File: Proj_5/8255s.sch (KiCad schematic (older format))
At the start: 18 parts, among them U1 8255, U2 8255, U3 8255

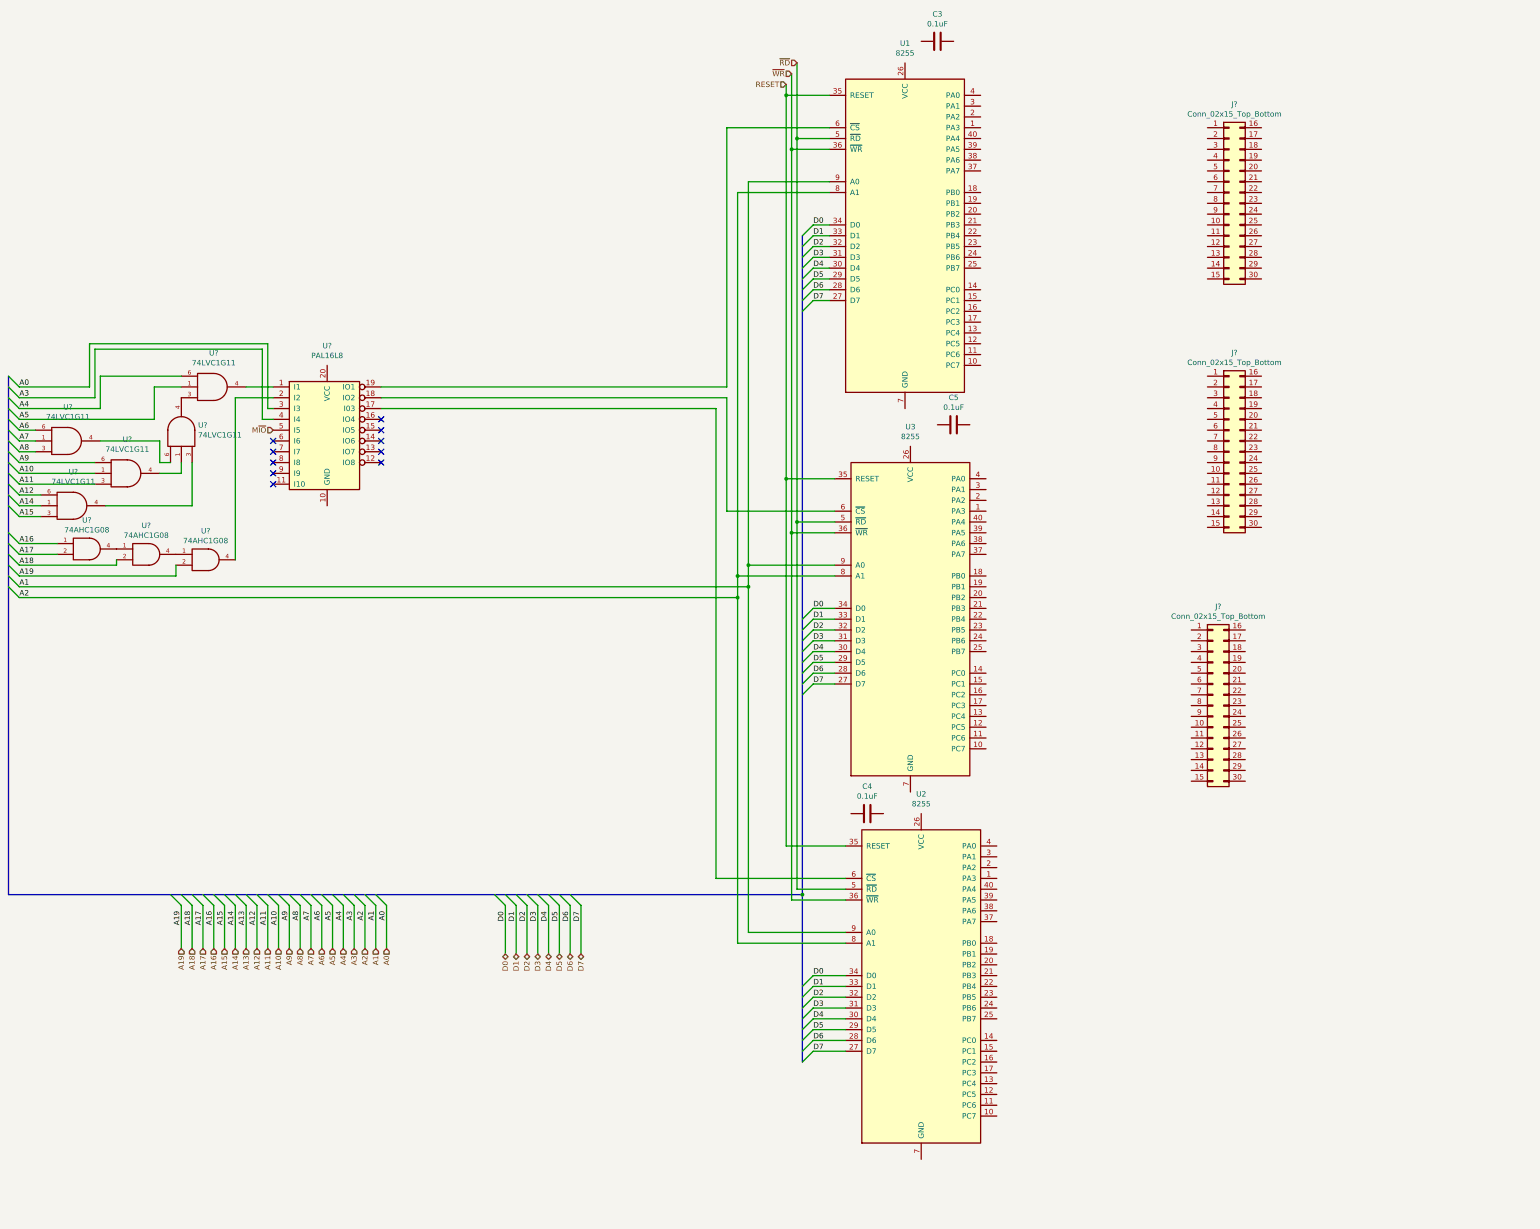
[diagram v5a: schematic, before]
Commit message: Rerouted Ext Wires, UART Mostly Complete, All Headers Added
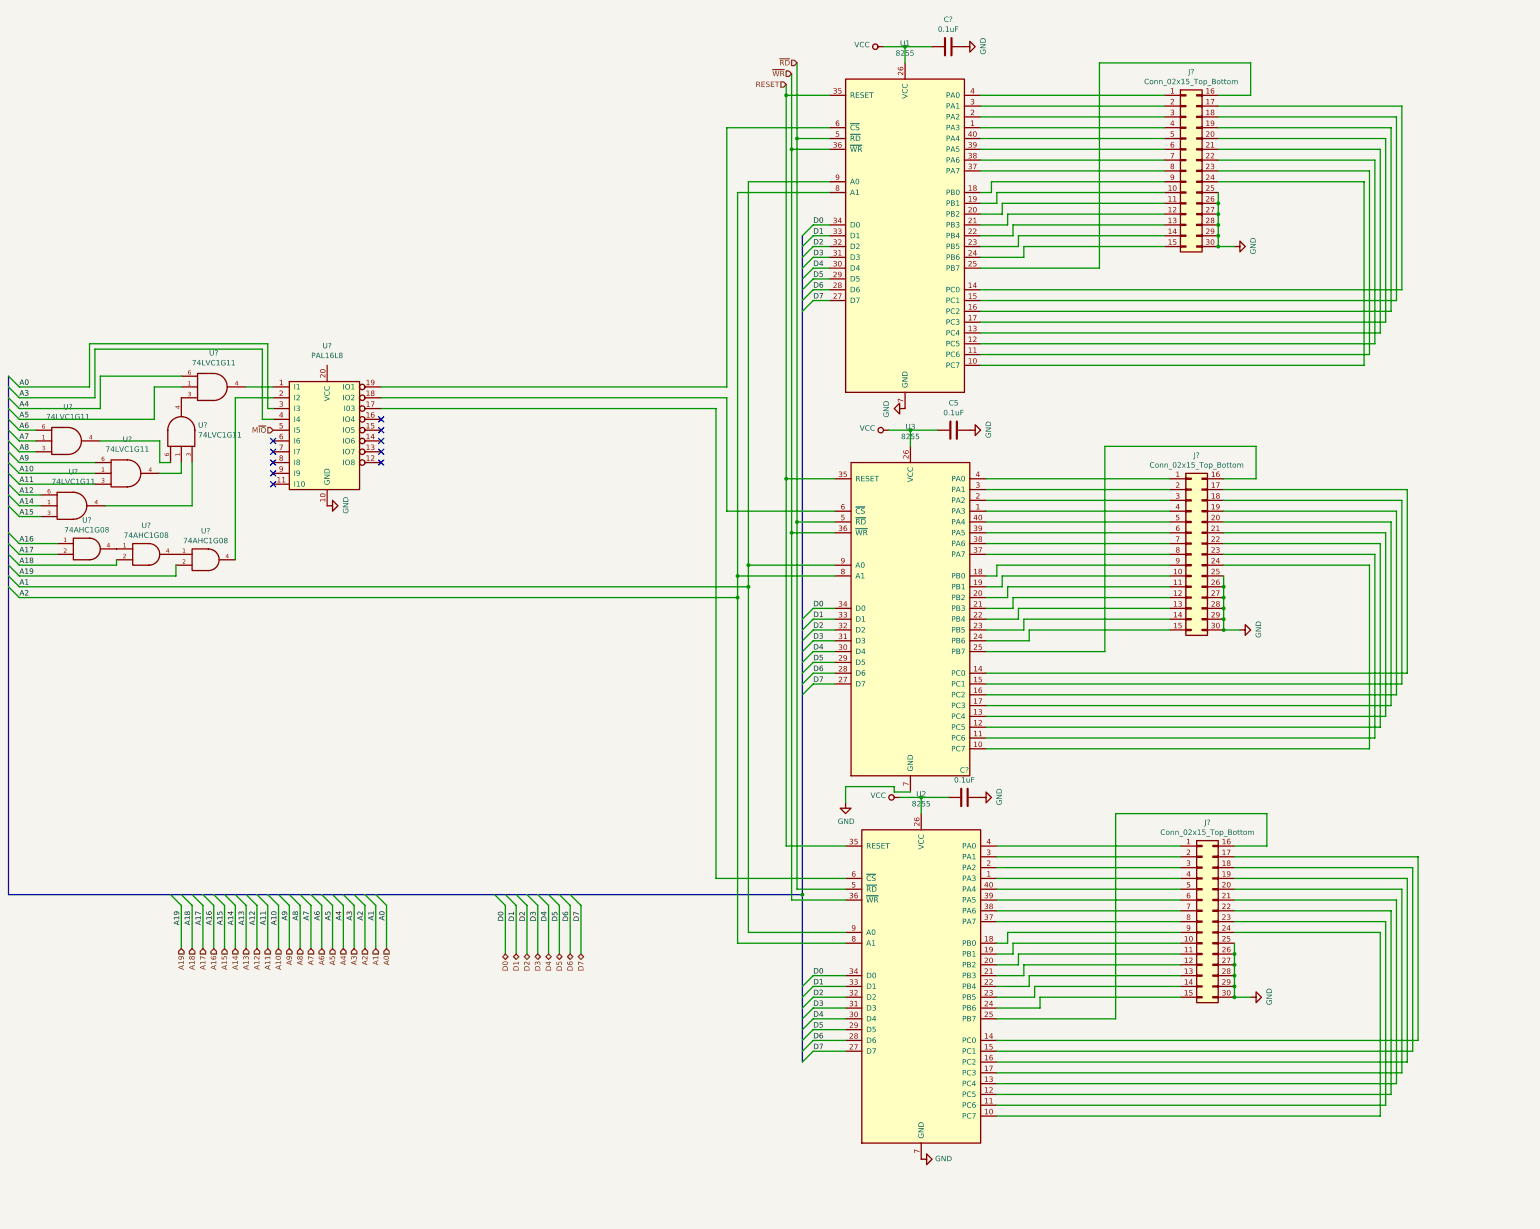
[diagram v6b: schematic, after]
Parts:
- removed C3, C4: 0.1uF, symbol Device:C
- removed J? (x2): Conn_02x15_Top_Bottom, symbol Connector_Generic:Conn_02x15_Top_Bottom
- added C? (x2): 0.1uF, symbol Device:C
- added J? (x2): Conn_02x15_Top_Bottom, symbol Connector_Generic:Conn_02x15_Top_Bottom
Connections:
- net GND: now also C5.1, J?.25 (Pin_25), J?.26 (Pin_26), J?.27 (Pin_27), J?.28 (Pin_28), J?.29 (Pin_29), J?.30 (Pin_30), U1.7 (GND), U2.7 (GND), U3.7 (GND), U?.10 (GND), C?.1, C?.1, J?.25 (Pin_25), J?.25 (Pin_25), J?.26 (Pin_26), J?.26 (Pin_26), J?.27 (Pin_27), J?.27 (Pin_27), J?.28 (Pin_28), J?.28 (Pin_28), J?.29 (Pin_29), J?.29 (Pin_29), J?.30 (Pin_30), J?.30 (Pin_30)
- net VCC: now also C5.2, U1.26 (VCC), U2.26 (VCC), U3.26 (VCC), C?.2, C?.2
- net at U1.1 (PA3): now also J?.4 (Pin_4)
- net at U1.10 (PC7): now also J?.24 (Pin_24)
- net at U1.11 (PC6): now also J?.23 (Pin_23)
- net at U1.12 (PC5): now also J?.22 (Pin_22)
- net at U1.13 (PC4): now also J?.21 (Pin_21)
- net at U1.14 (PC0): now also J?.17 (Pin_17)
- net at U1.15 (PC1): now also J?.18 (Pin_18)
- net at U1.16 (PC2): now also J?.19 (Pin_19)
- net at U1.17 (PC3): now also J?.20 (Pin_20)
- net at U1.18 (PB0): now also J?.9 (Pin_9)
- net at U1.19 (PB1): now also J?.10 (Pin_10)
- net at U1.2 (PA2): now also J?.3 (Pin_3)
- net at U1.20 (PB2): now also J?.11 (Pin_11)
- net at U1.21 (PB3): now also J?.12 (Pin_12)
- net at U1.22 (PB4): now also J?.13 (Pin_13)
- net at U1.23 (PB5): now also J?.14 (Pin_14)
- net at U1.24 (PB6): now also J?.15 (Pin_15)
- net at U1.25 (PB7): now also J?.16 (Pin_16)
- net at U1.3 (PA1): now also J?.2 (Pin_2)
- net at U1.37 (PA7): now also J?.8 (Pin_8)
- net at U1.38 (PA6): now also J?.7 (Pin_7)
- net at U1.39 (PA5): now also J?.6 (Pin_6)
- net at U1.4 (PA0): now also J?.1 (Pin_1)
- net at U1.40 (PA4): now also J?.5 (Pin_5)
- net at U2.1 (PA3): now also J?.4 (Pin_4)
- net at U2.10 (PC7): now also J?.24 (Pin_24)
- net at U2.11 (PC6): now also J?.23 (Pin_23)
- net at U2.12 (PC5): now also J?.22 (Pin_22)
- net at U2.13 (PC4): now also J?.21 (Pin_21)
- net at U2.14 (PC0): now also J?.17 (Pin_17)
- net at U2.15 (PC1): now also J?.18 (Pin_18)
- net at U2.16 (PC2): now also J?.19 (Pin_19)
- net at U2.17 (PC3): now also J?.20 (Pin_20)
- net at U2.18 (PB0): now also J?.9 (Pin_9)
- net at U2.19 (PB1): now also J?.10 (Pin_10)
- net at U2.2 (PA2): now also J?.3 (Pin_3)
- net at U2.20 (PB2): now also J?.11 (Pin_11)
- net at U2.21 (PB3): now also J?.12 (Pin_12)
- net at U2.22 (PB4): now also J?.13 (Pin_13)
- net at U2.23 (PB5): now also J?.14 (Pin_14)
- net at U2.24 (PB6): now also J?.15 (Pin_15)
- net at U2.25 (PB7): now also J?.16 (Pin_16)
- net at U2.3 (PA1): now also J?.2 (Pin_2)
- net at U2.37 (PA7): now also J?.8 (Pin_8)
- net at U2.38 (PA6): now also J?.7 (Pin_7)
- net at U2.39 (PA5): now also J?.6 (Pin_6)
- net at U2.4 (PA0): now also J?.1 (Pin_1)
- net at U2.40 (PA4): now also J?.5 (Pin_5)
- net at U3.1 (PA3): now also J?.4 (Pin_4)
- net at U3.10 (PC7): now also J?.24 (Pin_24)
- net at U3.11 (PC6): now also J?.23 (Pin_23)
- net at U3.12 (PC5): now also J?.22 (Pin_22)
- net at U3.13 (PC4): now also J?.21 (Pin_21)
- net at U3.14 (PC0): now also J?.17 (Pin_17)
- net at U3.15 (PC1): now also J?.18 (Pin_18)
- net at U3.16 (PC2): now also J?.19 (Pin_19)
- net at U3.17 (PC3): now also J?.20 (Pin_20)
- net at U3.18 (PB0): now also J?.9 (Pin_9)
- net at U3.19 (PB1): now also J?.10 (Pin_10)
- net at U3.2 (PA2): now also J?.3 (Pin_3)
- net at U3.20 (PB2): now also J?.11 (Pin_11)
- net at U3.21 (PB3): now also J?.12 (Pin_12)
- net at U3.22 (PB4): now also J?.13 (Pin_13)
- net at U3.23 (PB5): now also J?.14 (Pin_14)
- net at U3.24 (PB6): now also J?.15 (Pin_15)
- net at U3.25 (PB7): now also J?.16 (Pin_16)
- net at U3.3 (PA1): now also J?.2 (Pin_2)
- net at U3.37 (PA7): now also J?.8 (Pin_8)
- net at U3.38 (PA6): now also J?.7 (Pin_7)
- net at U3.39 (PA5): now also J?.6 (Pin_6)
- net at U3.4 (PA0): now also J?.1 (Pin_1)
- net at U3.40 (PA4): now also J?.5 (Pin_5)
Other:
- moved on the sheet: C5, J?

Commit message: Added Power Flags, finished no connects.
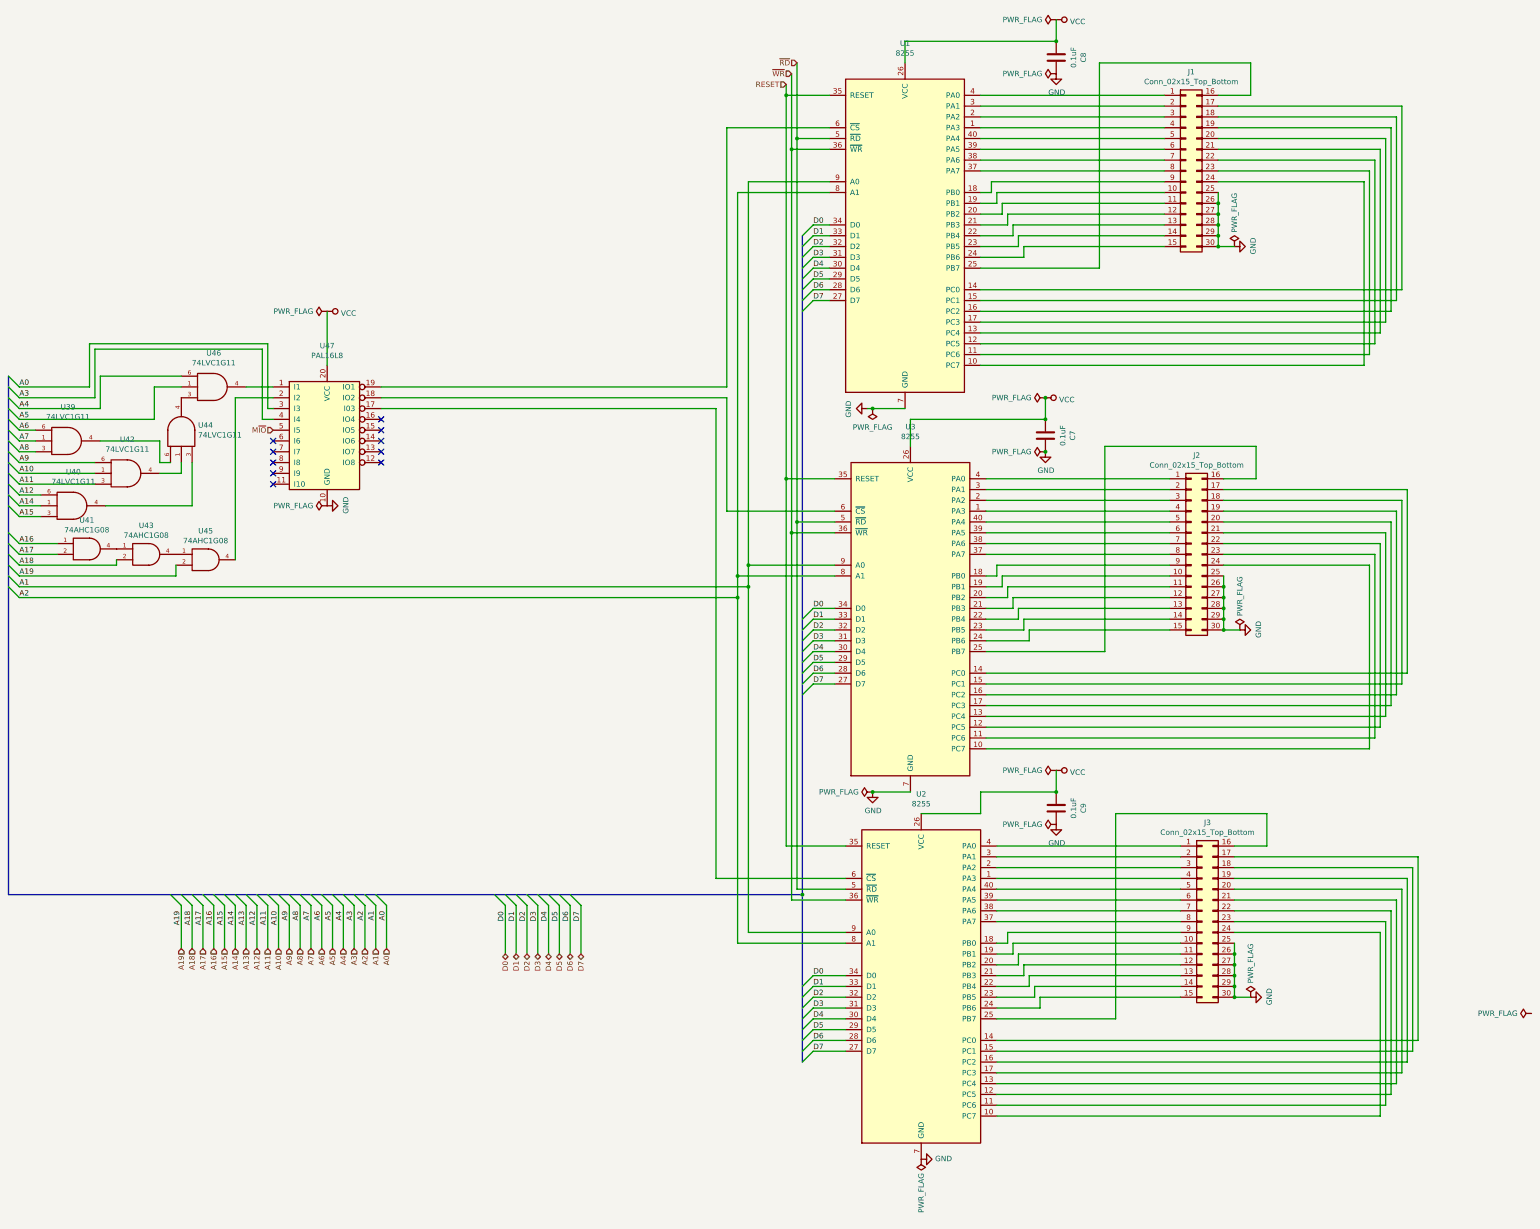
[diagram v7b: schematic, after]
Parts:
- removed C5, C?: 0.1uF, symbol Device:C
- added C7, C8: 0.1uF, symbol Device:C
- gave numbers to parts that had none: 13
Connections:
- net GND: now also C7.1, C8.1
- net VCC: now also U47.20 (VCC), C7.2, C8.2
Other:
- moved on the sheet: C9
